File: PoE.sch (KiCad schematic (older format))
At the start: 24 parts, among them IC1 TPS2378DDA

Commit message: Add review comments
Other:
- note added: "DNP should be visible for R52 and R53"
- note added: "What about APD? This circuit may be powered from other than PoE source.\n\nConsider adding an DC input (barrel jack or screw terminal) and calculate Rapd1/Rapd2 (chapter 8.2 of the datasheet)\nIf APD is not used tie it to GND to disable this functionality.\n\nAux power input can be especially helpful when debugging"
- note added: "What is purpose of this diode?\nLooking at datasheet, RTN signal \nshould be connected directly \nto GND\n(RTN becomes our reference signal)"
- note added: "should SNPS_CTRL be tied directly to GNDD?\nThen R55 and R56 are not needed\nAlternatively remove direct tie to the GND and make one of resistors DNP"
- note removed: "What about APD? This circuit may be powered from other than PoE source."
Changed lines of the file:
@@
 Wire Wire Line
 	5600 5300 5450 5300
-$Comp
-L antmicroResistors0402:R_0R_0402 R52
-U 1 1 61A460AF
-P 5850 4900
-F 0 "R52" H 5850 5113 60  0000 C CNN
-F 1 "R_0R_0402" H 5850 4750 60  0001 C CNN
-F 2 "antmicro-footprints:0402-res" H 6050 5100 60  0001 L CNN
-F 3 "" H 5850 4900 50  0001 C CNN
-F 4 "PANASONIC" H 6050 5300 60  0001 L CNN "Manufacturer"
-F 5 "ERJ2GE0R00X" H 6050 5200 60  0001 L CNN "MPN"
-F 6 "0R" H 5850 5015 50  0000 C CNN "Val"
-F 7 "DNP" H 5850 4900 50  0001 C CNN "DNP"
-	1    5850 4900
-	1    0    0    -1
-$EndComp
 Text GLabel 7250 2100 2    50   Input ~ 0
 APD
-Text Notes 14950 6400 0    50   ~ 0
-What about APD? This circuit may be powered from other than PoE source.
+Text Notes 4750 1450 0    50   ~ 0
+What about APD? This circuit may be powered from other than PoE source.\n\nConsider adding an DC input (barrel jack or screw terminal) and calculate Rapd1/Rapd2 (chapter 8.2 of the datasheet)\nIf APD is not used tie it to GND to disable this functionality.\n\nAux power input can be especially helpful when debugging
 Wire Wire Line
 	6750 2400 7950 2400
@@
 Wire Wire Line
 	6100 4900 6100 5100
-Text Notes 14800 6200 0    50   ~ 0
+Text Notes 4750 900  0    50   ~ 0
 REMARK:Typical aplication circuit can be found in \nTPS2378DDA datasheet:\n https://www.ti.com/lit/ds/symlink/tps2378.pdf?ts=1637556069032&ref_url=https%253A%252F%252Fwww.google.com%252F\nThere is the reference connection for APD circuit.
 Wire Wire Line
@@
 Text Label 1850 4750 1    50   ~ 0
 VDD
+Text Notes 7375 3475 0    50   ~ 0
+What is purpose of this diode?\nLooking at datasheet, RTN signal \nshould be connected directly \nto GND\n(RTN becomes our reference signal)
+Text Notes 9250 3250 0    50   ~ 0
+should SNPS_CTRL be tied directly to GNDD?\nThen R55 and R56 are not needed\nAlternatively remove direct tie to the GND and make one of resistors DNP
+$Comp
+L antmicroResistors0402:R_0R_0402 R52
+U 1 1 61A460AF
+P 5850 4900
+F 0 "R52" H 5850 5113 60  0000 C CNN
+F 1 "R_0R_0402" H 5850 4750 60  0001 C CNN
+F 2 "antmicro-footprints:0402-res" H 6050 5100 60  0001 L CNN
+F 3 "" H 5850 4900 50  0001 C CNN
+F 4 "PANASONIC" H 6050 5300 60  0001 L CNN "Manufacturer"
+F 5 "ERJ2GE0R00X" H 6050 5200 60  0001 L CNN "MPN"
+F 6 "0R" H 5850 5015 50  0000 C CNN "Val"
+F 7 "DNP" H 5850 4900 50  0001 C CNN "DNP"
+	1    5850 4900
+	1    0    0    -1
+$EndComp
+Text Notes 5275 4575 0    50   ~ 0
+DNP should be visible for R52 and R53
 $EndSCHEMATC

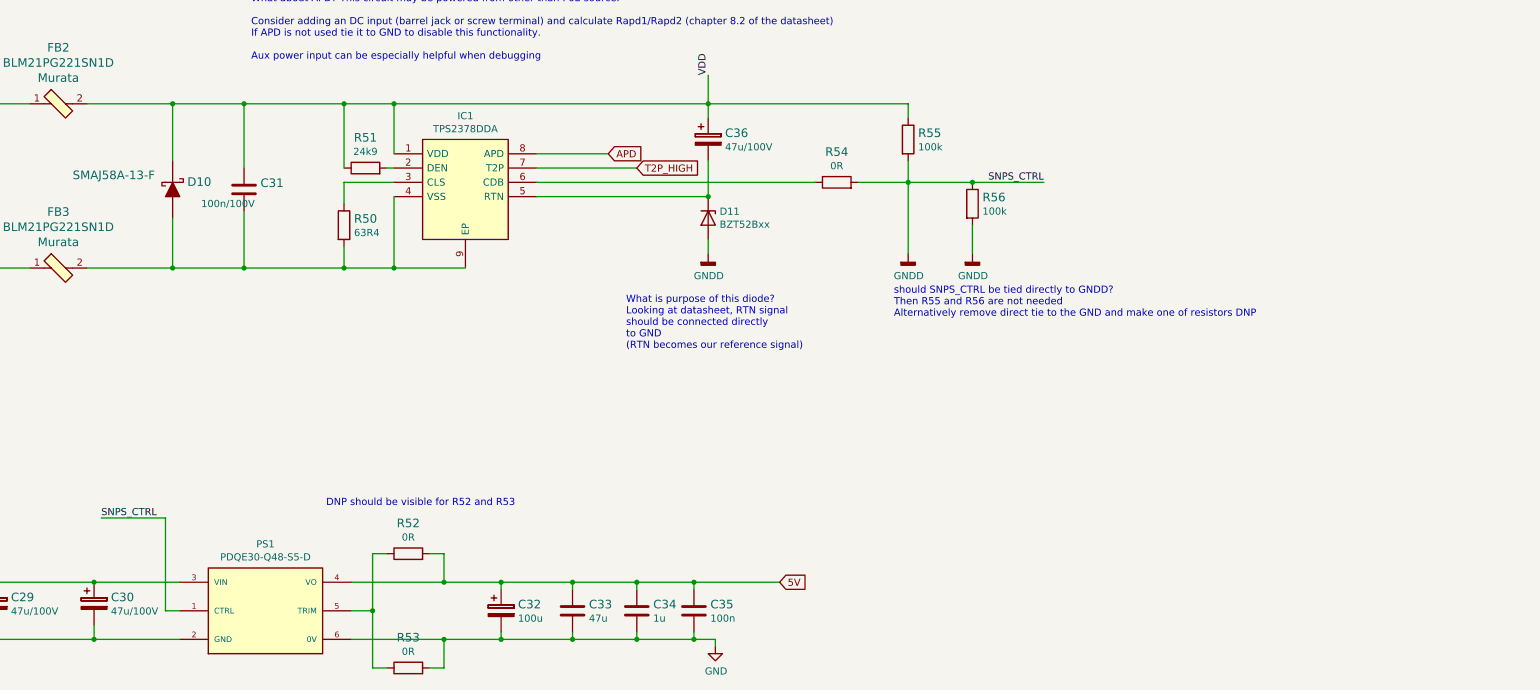
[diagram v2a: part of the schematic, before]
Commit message: added current limiting transistor circuit for poe controller
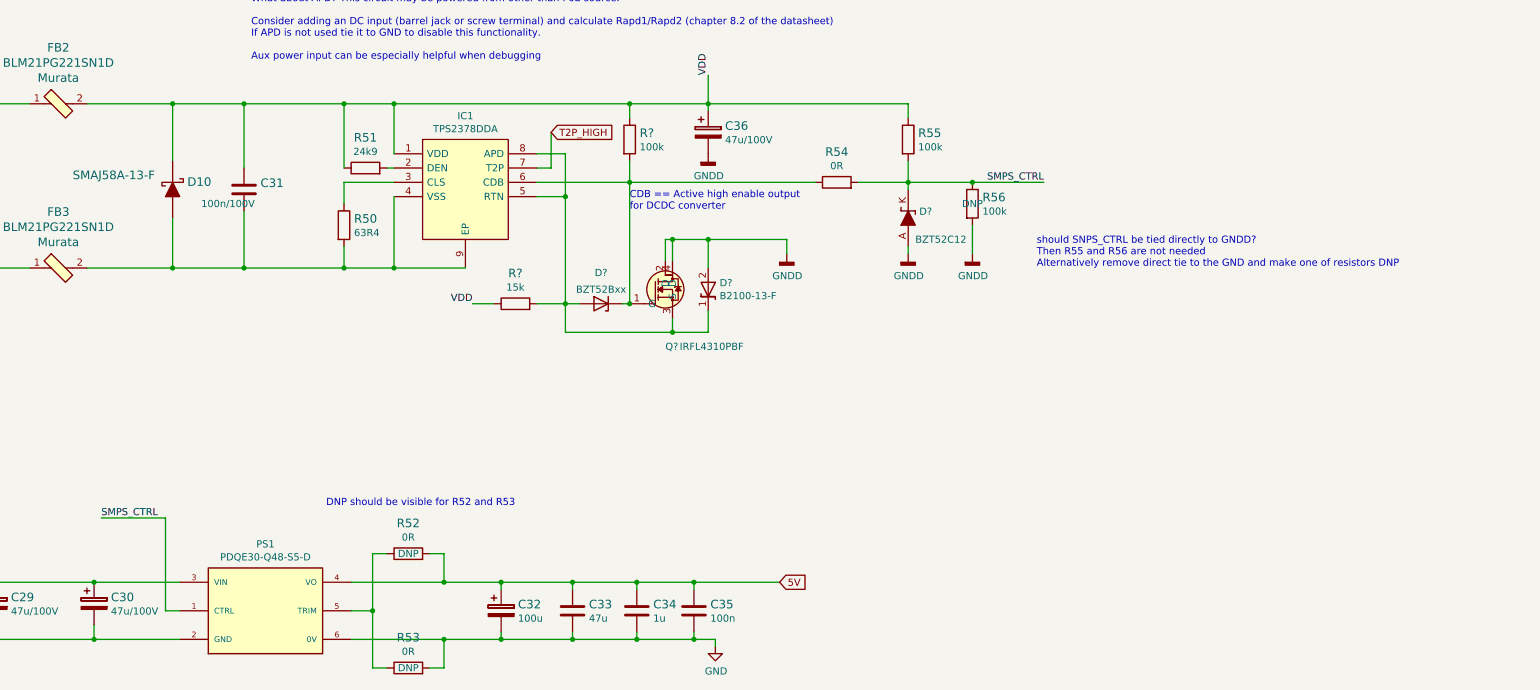
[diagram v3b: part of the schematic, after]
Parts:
- removed D11: BZT52Bxx, antmicro-footprints:SOD-123, symbol antmicroDiodesZenerSingle:BZT52Bxx
- added D?: BZT52C12, antmicro-footprints:SOD-123, symbol antmicroDiodesZenerSingle:BZT52C12
- added D?: BZT52Bxx, antmicro-footprints:SOD-123, symbol antmicroDiodesZenerSingle:BZT52Bxx
- added D?: B2100-13-F, antmicro-footprints:DIOM5336X250N, symbol antmicroDiodesRectifiersSingle:B2100-13-F
- added Q?: IRFL4310PBF, antmicro-footprint:SOT230P700X180-4N, symbol antmicroTransistorsFETsMOSFETsSingle:IRFL4310PBF
- added R?: R_100k_0402, antmicro-footprints:0402-res, symbol antmicroResistors0402:R_100k_0402
- added R?: R_15k_0603, antmicro-footprints:0603-res, symbol antmicroResistors0603:R_15k_0603
- R56: DNP (none) -> DNP
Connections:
- net APD is gone; now on an unnamed net: IC1.8 (APD)
- net GNDD: now also C36.2, D?.2, D?.A, Q?.2 (D), Q?.4 (D); no longer PS1.1 (CTRL), R54.2, R55.2, R56.1
- net VDD: now also R?.1, R?.1
- net at IC1.5 (RTN): now also D?.1, D?.A, Q?.3 (S), R?.2; no longer C36.2
- net at IC1.6 (CDB), R54.1: now also D?.K, Q?.1 (G), R?.2
- new net SMPS_CTRL: D?.K, PS1.1 (CTRL), R54.2, R55.2, R56.1
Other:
- note added: "CDB == Active high enable output \nfor DCDC converter"
- note removed: "What is purpose of this diode?\nLooking at datasheet, RTN signal \nshould be connected directly \nto GND\n(RTN becomes our reference signal)"
- moved on the sheet: C36
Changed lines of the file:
@@
 	5400 2900 5750 2900
-Wire Wire Line
-	7950 2800 7950 2700
 Wire Wire Line
 	1450 2600 1650 2600
@@
 Wire Wire Line
 	5600 5300 5450 5300
-Text GLabel 7250 2100 2    50   Input ~ 0
-APD
 Text Notes 4750 1450 0    50   ~ 0
 What about APD? This circuit may be powered from other than PoE source.\n\nConsider adding an DC input (barrel jack or screw terminal) and calculate Rapd1/Rapd2 (chapter 8.2 of the datasheet)\nIf APD is not used tie it to GND to disable this functionality.\n\nAux power input can be especially helpful when debugging
 Wire Wire Line
-	6750 2400 7950 2400
-Wire Wire Line
 	3700 4650 4150 4650
 Text Label 3700 4650 0    50   ~ 0
-SNPS_CTRL
+SMPS_CTRL
 Wire Wire Line
 	4150 5300 4150 4650
@@
 	9800 2300 10300 2300
 Text Label 10300 2300 2    50   ~ 0
-SNPS_CTRL
+SMPS_CTRL
 Connection ~ 9800 2300
 Connection ~ 2950 5500
@@
 Wire Wire Line
 	9800 2600 9800 2800
-Wire Wire Line
-	9350 2300 9350 2800
 $Comp
 L power:GNDD #PWR046
@@
 F 5 "CRCW0402100KFKEDHP" H 10000 2750 60  0001 L CNN "MPN"
 F 6 "100k" V 9853 2520 50  0000 L CNN "Val"
+F 7 "DNP" V 9800 2450 50  0000 C CNN "DNP"
 	1    9800 2450
 	0    1    1    0
 $EndComp
-$Comp
-L antmicroDiodesZenerSingle:BZT52Bxx D11
-U 1 1 61A46110
-P 7950 2550
-F 0 "D11" V 7904 2630 50  0000 L CNN
-F 1 "BZT52Bxx" V 7995 2630 50  0000 L CNN
-F 2 "antmicro-footprints:SOD-123" H 7950 2375 50  0001 C CNN
-F 3 "https://diotec.com/tl_files/diotec/files/pdf/datasheets/bzt52b2v4.pdf" H 7950 2550 50  0001 C CNN
-F 4 "BZT52C18-G3-18" H 7975 2300 50  0001 C CNN "MPN"
-F 5 "Vishay" H 7950 2200 50  0001 C CNN "Manufacturer"
-	1    7950 2550
-	0    1    1    0
-$EndComp
-Connection ~ 7950 2400
 Wire Wire Line
 	7950 1750 7950 1550
-Wire Wire Line
-	7950 2150 7950 2400
 $Comp
 L antmicroCapacitorspol:C_47u_ELEC_100V C36
 U 1 1 61A4611D
-P 7950 1950
-F 0 "C36" H 8068 1945 60  0000 L CNN
-F 1 "C_47u_ELEC_100V" H 7950 1800 60  0001 C CNN
-F 2 "antmicro-footprints:CP_Elec_10x10.5" H 8150 2150 60  0001 L CNN
-F 3 "https://industrial.panasonic.com/cdbs/www-data/pdf/RDE0000/ABA0000C1151.pdf" H 7950 1950 50  0001 C CNN
-F 4 "PANASONIC" H 8150 2350 60  0001 L CNN "Manufacturer"
-F 5 "EEEHA2A470UP" H 8150 2250 60  0001 L CNN "MPN"
-F 6 "47u/100V" H 8068 1847 50  0000 L CNN "Val"
-	1    7950 1950
+P 7950 1900
+F 0 "C36" H 8068 1895 60  0000 L CNN
+F 1 "C_47u_ELEC_100V" H 7950 1750 60  0001 C CNN
+F 2 "antmicro-footprints:CP_Elec_10x10.5" H 8150 2100 60  0001 L CNN
+F 3 "https://industrial.panasonic.com/cdbs/www-data/pdf/RDE0000/ABA0000C1151.pdf" H 7950 1900 50  0001 C CNN
+F 4 "PANASONIC" H 8150 2300 60  0001 L CNN "Manufacturer"
+F 5 "EEEHA2A470UP" H 8150 2200 60  0001 L CNN "MPN"
+F 6 "47u/100V" H 8068 1797 50  0000 L CNN "Val"
+	1    7950 1900
 	1    0    0    -1
 $EndComp
@@
 L power:GNDD #PWR043
 U 1 1 61A46129
-P 7950 2800
-F 0 "#PWR043" H 7950 2550 50  0001 C CNN
-F 1 "GNDD" H 7954 2645 50  0000 C CNN
-F 2 "" H 7950 2800 50  0001 C CNN
-F 3 "" H 7950 2800 50  0001 C CNN
-	1    7950 2800
+P 8500 2800
+F 0 "#PWR043" H 8500 2550 50  0001 C CNN
+F 1 "GNDD" H 8504 2645 50  0000 C CNN
+F 2 "" H 8500 2800 50  0001 C CNN
+F 3 "" H 8500 2800 50  0001 C CNN
+	1    8500 2800
 	1    0    0    -1
 $EndComp
@@
 $EndComp
 Wire Wire Line
-	7950 1750 7950 1850
-Wire Wire Line
-	6750 2300 8700 2300
+	7950 1750 7950 1800
+Wire Wire Line
+	6750 2300 7400 2300
 Connection ~ 5400 2900
 Wire Wire Line
@@
 Connection ~ 5750 1750
 Wire Wire Line
-	5750 1750 7950 1750
-Wire Wire Line
-	6750 2200 7450 2200
-Text GLabel 7450 2200 2    50   Input ~ 0
-T2P_HIGH
-Wire Wire Line
-	6750 2100 7250 2100
+	5750 1750 7400 1750
+Wire Wire Line
+	6750 2100 6950 2100
 $Comp
 L antmicroResistors0402:R_0R_0402 R53
@@
 F 5 "ERJ2GE0R00X" H 6050 6000 60  0001 L CNN "MPN"
 F 6 "0R" H 5850 5815 50  0000 C CNN "Val"
-F 7 "DNP" H 5850 5700 50  0001 C CNN "DNP"
+F 7 "DNP" H 5850 5700 50  0000 C CNN "DNP"
 	1    5850 5700
 	1    0    0    -1
@@
 Text Label 1850 4750 1    50   ~ 0
 VDD
-Text Notes 7375 3475 0    50   ~ 0
-What is purpose of this diode?\nLooking at datasheet, RTN signal \nshould be connected directly \nto GND\n(RTN becomes our reference signal)
-Text Notes 9250 3250 0    50   ~ 0
+Text Notes 10250 2900 0    50   ~ 0
 should SNPS_CTRL be tied directly to GNDD?\nThen R55 and R56 are not needed\nAlternatively remove direct tie to the GND and make one of resistors DNP
 $Comp
@@
 F 5 "ERJ2GE0R00X" H 6050 5200 60  0001 L CNN "MPN"
 F 6 "0R" H 5850 5015 50  0000 C CNN "Val"
-F 7 "DNP" H 5850 4900 50  0001 C CNN "DNP"
+F 7 "DNP" H 5850 4900 50  0000 C CNN "DNP"
 	1    5850 4900
 	1    0    0    -1
@@
 Text Notes 5275 4575 0    50   ~ 0
 DNP should be visible for R52 and R53
+$Comp
+L antmicroDiodesZenerSingle:BZT52C12 D?
+U 1 1 6286AAC9
+P 9350 2550
+F 0 "D?" V 9396 2472 50  0000 R CNN
+F 1 "BZT52C12" V 9200 2500 50  0000 R CNN
+F 2 "antmicro-footprints:SOD-123" H 9350 2550 50  0001 C CNN
+F 3 "https://www.farnell.com/datasheets/1670962.pdf" H 9350 2550 50  0001 C CNN
+F 4 "BZT52C12" H 9350 2550 50  0001 C CNN "MPN"
+F 5 "DIODES INC." H 9350 2550 50  0001 C CNN "Manufacturer"
+	1    9350 2550
+	0    -1   -1   0
+$EndComp
+Text Notes 7400 2500 0    50   ~ 0
+CDB == Active high enable output \nfor DCDC converter
+Wire Wire Line
+	9350 2750 9350 2800
+Wire Wire Line
+	9350 2350 9350 2300
+$Comp
+L antmicroTransistorsFETsMOSFETsSingle:IRFL4310PBF Q?
+U 1 1 62893844
+P 7100 3050
+F 0 "Q?" H 7650 2650 50  0000 L CNN
+F 1 "IRFL4310PBF" H 7750 2650 50  0000 L CNN
+F 2 "antmicro-footprint:SOT230P700X180-4N" H 7950 3150 50  0001 L CNN
+F 3 "https://www.infineon.com/dgdl/irfl4310pbf.pdf?fileId=5546d462533600a40153562804ba1fbc" H 7950 3050 50  0001 L CNN
+F 4 "MOSFET N-Channel 100V 2.2A SOT223 International Rectifier IRFL4310PBF N-channel MOSFET Transistor, 2.2 A, 100 V, 4-Pin SOT-223" H 7950 2950 50  0001 L CNN "Description"
+F 5 "Infineon" H 7950 2750 50  0001 L CNN "Manufacturer"
+F 6 "IRFL4310PBF" H 7950 2650 50  0001 L CNN "MPN"
+	1    7100 3050
+	1    0    0    -1
+$EndComp
+Wire Wire Line
+	6950 2100 6950 2400
+Wire Wire Line
+	6750 2400 6950 2400
+$Comp
+L antmicroDiodesZenerSingle:BZT52Bxx D?
+U 1 1 628B62B3
+P 7200 3150
+F 0 "D?" H 7200 2933 50  0000 C CNN
+F 1 "BZT52Bxx" H 7200 3050 50  0000 C CNN
+F 2 "antmicro-footprints:SOD-123" H 7200 2975 50  0001 C CNN
+F 3 "https://diotec.com/tl_files/diotec/files/pdf/datasheets/bzt52b2v4.pdf" H 7200 3150 50  0001 C CNN
+F 4 "BZT52C18-G3-18" H 7225 2900 50  0001 C CNN "MPN"
+F 5 "Vishay" H 7200 2800 50  0001 C CNN "Manufacturer"
+	1    7200 3150
+	-1   0    0    1
+$EndComp
+Wire Wire Line
+	7350 3150 7400 3150
+Wire Wire Line
+	6950 3150 7050 3150
+$Comp
+L antmicroDiodesRectifiersSingle:B2100-13-F D?
+U 1 1 628C2229
+P 7950 3400
+F 0 "D?" V 8346 3320 50  0000 R CNN
+F 1 "B2100-13-F" V 8255 3320 50  0000 R CNN
+F 2 "antmicro-footprints:DIOM5336X250N" H 8400 3400 50  0001 L CNN
+F 3 "https://componentsearchengine.com/Datasheets/2/B2100-13-F.pdf" H 8400 3300 50  0001 L CNN
+F 4 "MULTICOMP - B2100-13-F - RECTIFIER, SCHOTTKY, 2A, 100V, DO-214AA, FULL REEL" H 8400 3200 50  0001 L CNN "Description"
+F 5 "MULTICOMP" H 8400 3000 50  0001 L CNN "Manufacturer"
+F 6 "B2100-13-F" H 8400 2900 50  0001 L CNN "MPN"
+	1    7950 3400
+	0    -1   -1   0
+$EndComp
+Wire Wire Line
+	7650 2850 7650 2700
+Wire Wire Line
+	7650 2700 7700 2700
+Wire Wire Line
+	7700 2700 7700 2850
+Wire Wire Line
+	7700 2700 7950 2700
+Connection ~ 7700 2700
+Connection ~ 7950 2700
+Wire Wire Line
+	7950 3350 7700 3350
+Wire Wire Line
+	7700 3350 7700 3250
+Wire Wire Line
+	7700 3350 6950 3350
+Wire Wire Line
+	6950 3350 6950 3150
+Connection ~ 7700 3350
+Wire Wire Line
+	7950 2700 8500 2700
+Wire Wire Line
+	8500 2800 8500 2700
+$Comp
+L power:GNDD #PWR?
+U 1 1 628EFC20
+P 7950 2100
+F 0 "#PWR?" H 7950 1850 50  0001 C CNN
+F 1 "GNDD" H 7954 1945 50  0000 C CNN
+F 2 "" H 7950 2100 50  0001 C CNN
+F 3 "" H 7950 2100 50  0001 C CNN
+	1    7950 2100
+	1    0    0    -1
+$EndComp
+Wire Wire Line
+	7950 2700 7950 2900
+Wire Wire Line
+	7950 3200 7950 3350
+Connection ~ 7400 2300
+Wire Wire Line
+	7400 2300 8700 2300
+Text GLabel 6850 1950 2    50   Input ~ 0
+T2P_HIGH
+Wire Wire Line
+	6750 2200 6850 2200
+Wire Wire Line
+	6850 2200 6850 1950
+Wire Wire Line
+	7400 1850 7400 1750
+Connection ~ 7400 1750
+Wire Wire Line
+	7400 1750 7950 1750
+Wire Wire Line
+	7400 2150 7400 2300
+$Comp
+L antmicroResistors0402:R_100k_0402 R?
+U 1 1 6291111C
+P 7400 2000
+F 0 "R?" V 7355 2070 60  0000 L CNN
+F 1 "R_100k_0402" H 7400 1850 60  0001 C CNN
+F 2 "antmicro-footprints:0402-res" H 7600 2200 60  0001 L CNN
+F 3 "" H 7400 2000 50  0001 C CNN
+F 4 "VISHAY" H 7600 2400 60  0001 L CNN "Manufacturer"
+F 5 "CRCW0402100KFKEDHP" H 7600 2300 60  0001 L CNN "MPN"
+F 6 "100k" V 7453 2070 50  0000 L CNN "Val"
+	1    7400 2000
+	0    1    1    0
+$EndComp
+Connection ~ 6950 3150
+Wire Wire Line
+	6950 2400 6950 3150
+Connection ~ 7400 3150
+Wire Wire Line
+	7400 2300 7400 3150
+Connection ~ 6950 2400
+$Comp
+L antmicroResistors0603:R_15k_0603 R?
+U 1 1 629705A0
+P 6600 3150
+F 0 "R?" H 6600 3363 60  0000 C CNN
+F 1 "R_15k_0603" H 6600 3000 60  0001 C CNN
+F 2 "antmicro-footprints:0603-res" H 6800 3350 60  0001 L CNN
+F 3 "" H 6600 3150 50  0001 C CNN
+F 4 "BOURNS" H 6800 3550 60  0001 L CNN "Manufacturer"
+F 5 "CR0603-FX-1502ELF" H 6800 3450 60  0001 L CNN "MPN"
+F 6 "15k" H 6600 3265 50  0000 C CNN "Val"
+	1    6600 3150
+	1    0    0    -1
+$EndComp
+Wire Wire Line
+	6750 3150 6950 3150
+Wire Wire Line
+	6450 3150 6300 3150
+Text Label 6300 3150 2    50   ~ 0
+VDD
 $EndSCHEMATC

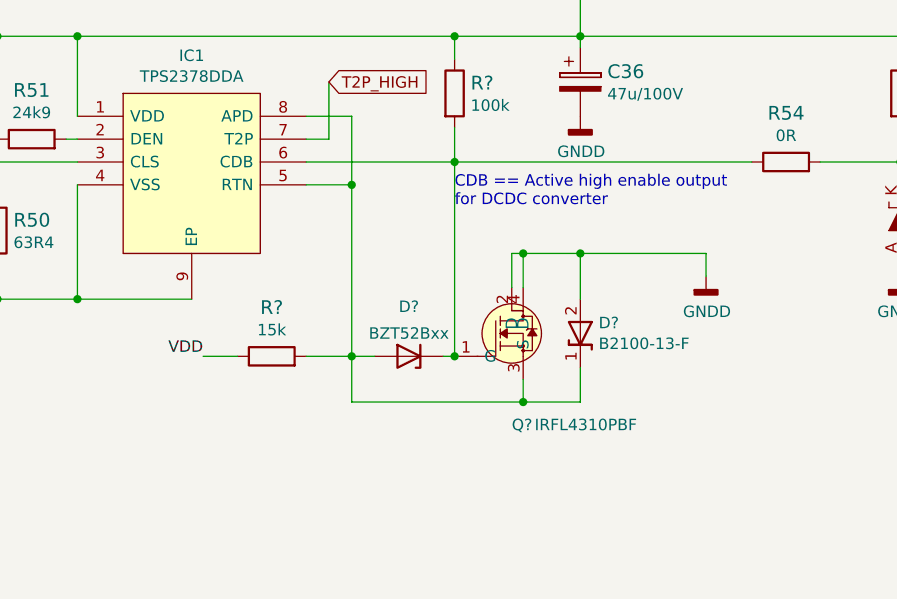
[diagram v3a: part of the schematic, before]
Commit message: removed transistor circtuit - work in progress
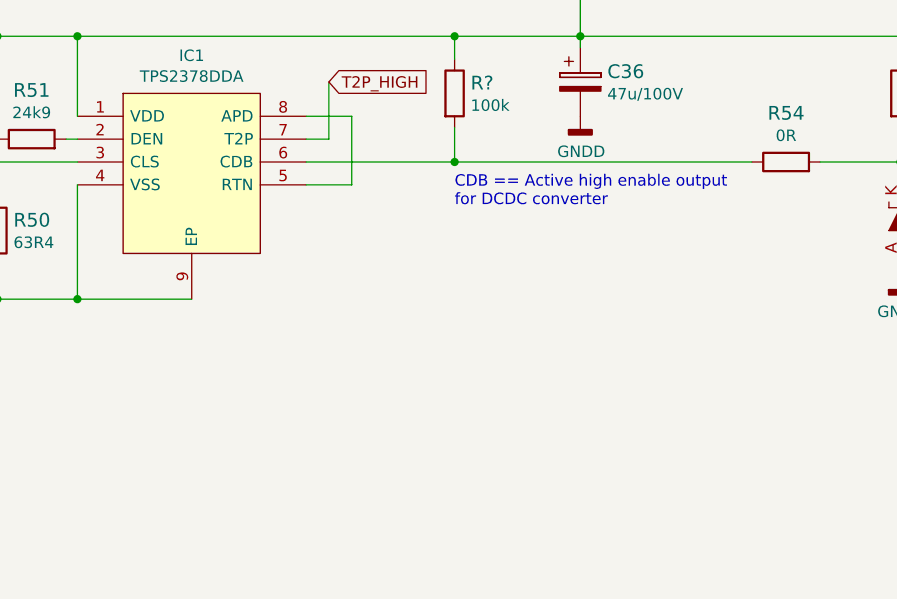
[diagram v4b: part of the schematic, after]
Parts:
- removed D?: BZT52Bxx, antmicro-footprints:SOD-123, symbol antmicroDiodesZenerSingle:BZT52Bxx
- removed D?: B2100-13-F, antmicro-footprints:DIOM5336X250N, symbol antmicroDiodesRectifiersSingle:B2100-13-F
- removed Q?: IRFL4310PBF, antmicro-footprint:SOT230P700X180-4N, symbol antmicroTransistorsFETsMOSFETsSingle:IRFL4310PBF
- removed R?: R_15k_0603, antmicro-footprints:0603-res, symbol antmicroResistors0603:R_15k_0603
